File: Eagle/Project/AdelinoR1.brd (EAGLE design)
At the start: 47 x 53.3 mm, 63 parts, among them J1 DC-044-A, J2 YELLOW-6P-2.54, J3 YELLOW-8P-2.54, J4 YELLOW-8P-2.54, J5 YELLOW-8P-2.54, Q1 NCE3407A, Q2 CJ2305, U1 ATMEGA32U4-TQFP44, U2 CJT1117-5.0-SOT223, U3 ESP-12F / OPL: 317060163 / SM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, U4 CJT1117-3.3-SOT223, X1 306010049_XTAL_16MHZ-3225_4P

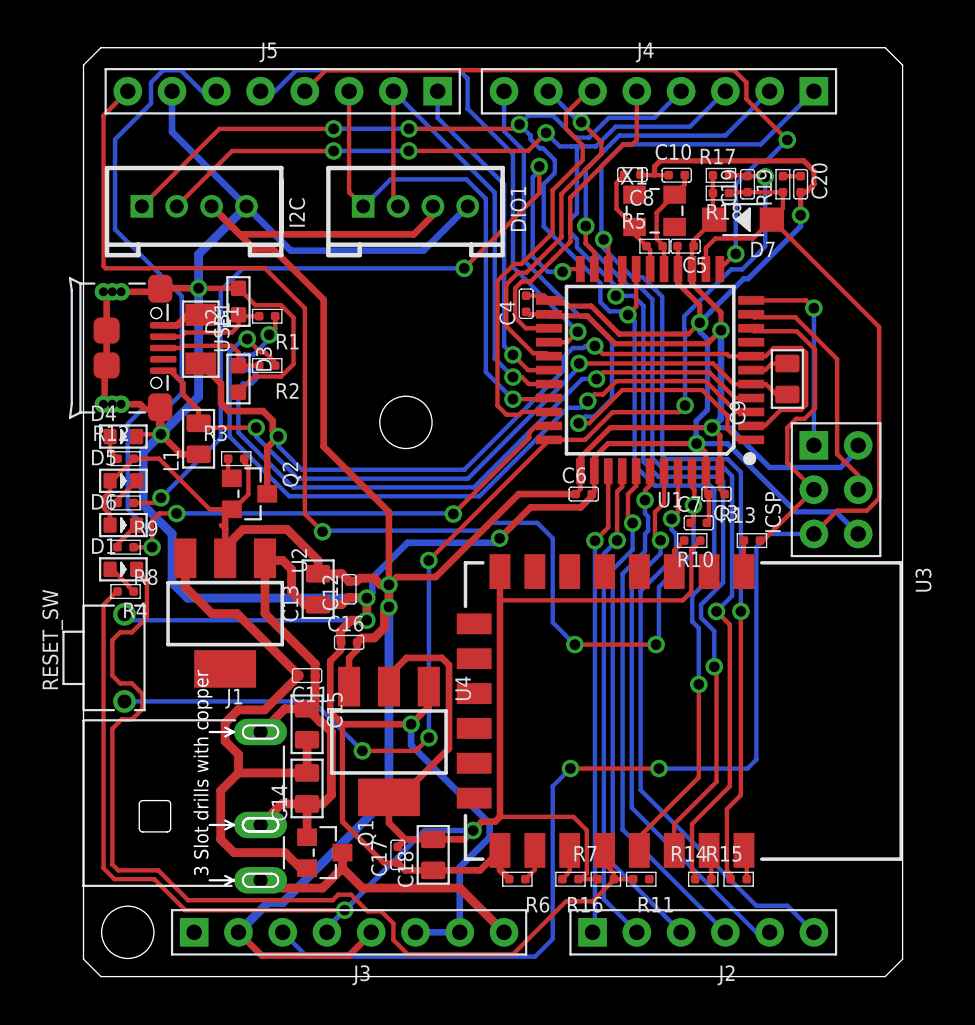
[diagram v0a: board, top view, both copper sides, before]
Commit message: Add MOSI->GPIO0 connection.
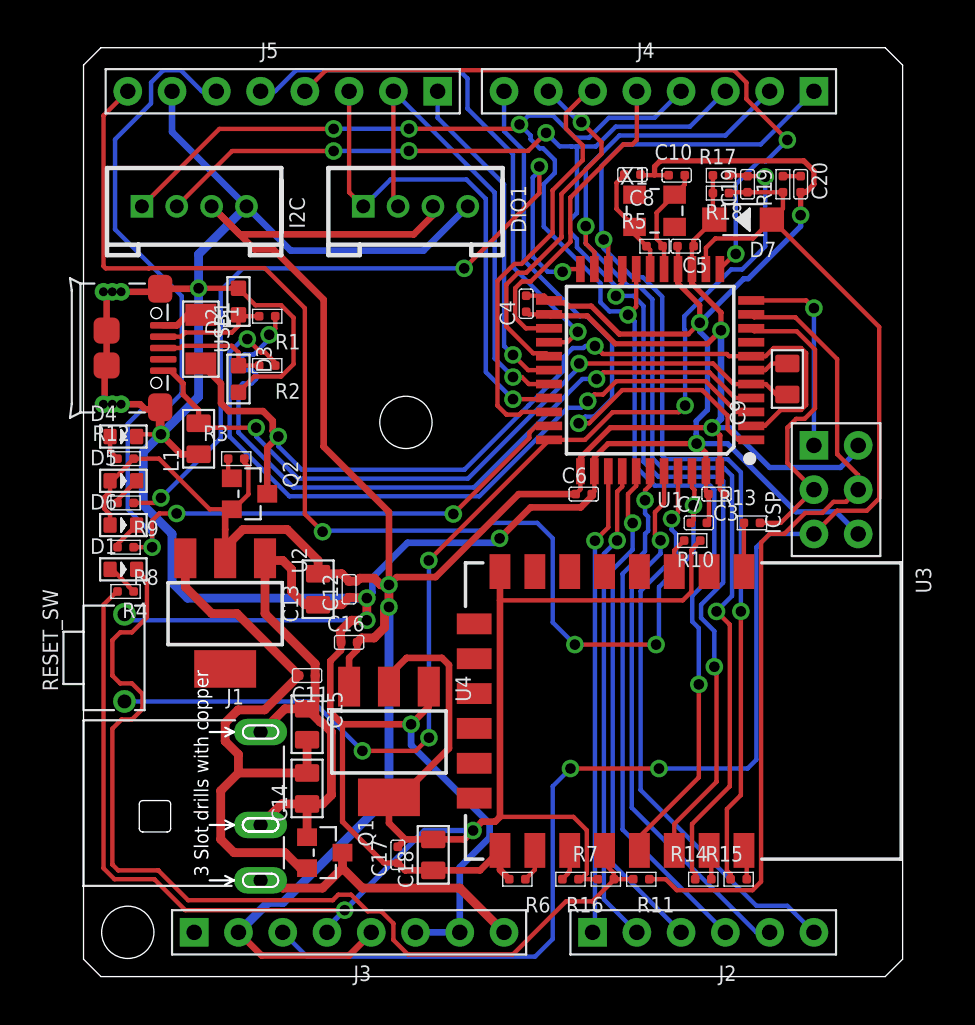
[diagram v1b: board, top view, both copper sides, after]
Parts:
- moved R13 1.02 mm to (38.4, 26.0)
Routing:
- net MOSI: track 14.0 -> 47.1 mm
- net N$14: track 1.78 -> 2.80 mm
- net GND: track 278.3 -> 278.8 mm
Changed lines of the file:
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@@
 <text x="18.0086" y="4.064" size="1.016" layer="136" font="vector" ratio="12">-GND-</text>
 <wire x1="13.97" y1="4.064" x2="13.97" y2="4.1148" width="0.1524" layer="136"/>
-<rectangle x1="38.862" y1="6.096" x2="46.99" y2="24.384" layer="41"/>
 <rectangle x1="38.862" y1="6.096" x2="46.99" y2="24.384" layer="42"/>
 <text x="4.064" y="31.877" size="0.8128" layer="136" font="vector" ratio="12" rot="SR270">PWR ACT D13 ESP</text>
@@
 www.neoautus.com
 Prototype only</text>
+<rectangle x1="39.116" y1="6.096" x2="46.99" y2="24.384" layer="41"/>
 </plain>
 <attributes>
@@
 <element name="C10" library="Seeed-Capacitor" package="C0402" value="22pf" x="34.036" y="45.9835" rot="R90">
 <attribute name="MPN" value="CC0402JRNPO9BN220" x="34.036" y="45.9835" size="1.778" layer="27" rot="R90" display="off"/>
+<attribute name="NAME" x="32.766" y="45.7295" size="0.635" layer="33" ratio="10"/>
 <attribute name="NAME" x="32.766" y="46.8725" size="0.889" layer="25" ratio="11"/>
-<attribute name="NAME" x="32.766" y="45.7295" size="0.635" layer="33" ratio="10"/>
 <attribute name="VALUE" x="32.766" y="44.396" size="0.635" layer="27" ratio="10"/>
 </element>
@@
 <element name="C8" library="Seeed-Capacitor" package="C0402" value="22pf" x="31.496" y="46.0195" rot="R270">
 <attribute name="MPN" value="CC0402JRNPO9BN220" x="31.496" y="46.0195" size="1.778" layer="27" rot="R270" display="off"/>
+<attribute name="NAME" x="32.766" y="46.2735" size="0.635" layer="33" ratio="10" rot="R180"/>
 <attribute name="NAME" x="32.766" y="45.1305" size="0.889" layer="25" ratio="11" rot="R180"/>
-<attribute name="NAME" x="32.766" y="46.2735" size="0.635" layer="33" ratio="10" rot="R180"/>
 <attribute name="VALUE" x="32.766" y="47.607" size="0.635" layer="27" ratio="10" rot="R180"/>
 </element>
@@
 <element name="J1" library="Seeed-Connector" package="DCJ3P-11.6X9.6X7.0MM" value="DC-044-A" x="0" y="9.906" rot="R270">
 <attribute name="MPN" value="JACK-DC-044-A" x="0" y="9.906" size="1.778" layer="27" rot="R270" display="off"/>
+<attribute name="NAME" x="6.985" y="13.1445" size="1.27" layer="33" ratio="10" rot="R270"/>
 <attribute name="NAME" x="8.1915" y="15.621" size="0.889" layer="25" ratio="11"/>
-<attribute name="NAME" x="6.985" y="13.1445" size="1.27" layer="33" ratio="10" rot="R270"/>
 <attribute name="VALUE" x="4.3815" y="3.556" size="0.889" layer="27" ratio="11"/>
 </element>
 <element name="J2" library="Seeed-Connector" package="H6-2.54" value="YELLOW-6P-2.54" x="35.56" y="2.54" rot="R90">
 <attribute name="MPN" value="F185-1106A1BSYA3" x="35.56" y="2.54" size="1.778" layer="27" rot="R90" display="off"/>
+<attribute name="NAME" x="38.1" y="3.175" size="0.635" layer="33" ratio="10" rot="R180"/>
 <attribute name="NAME" x="37.465" y="0.635" size="0.889" layer="25" ratio="11" rot="R180"/>
-<attribute name="NAME" x="38.1" y="3.175" size="0.635" layer="33" ratio="10" rot="R180"/>
 <attribute name="VALUE" x="37.465" y="5.08" size="0.889" layer="27" ratio="11" rot="R180"/>
 </element>
 <element name="J3" library="Seeed-Connector" package="H8-2.54" value="YELLOW-8P-2.54" x="15.24" y="2.54" rot="R90">
 <attribute name="MPN" value="F185-1108A1BSYC1" x="15.24" y="2.54" size="1.778" layer="27" rot="R90" display="off"/>
+<attribute name="NAME" x="15.875" y="2.54" size="0.3048" layer="33" ratio="10" rot="R180"/>
 <attribute name="NAME" x="16.51" y="0.635" size="0.889" layer="25" ratio="11" rot="R180"/>
-<attribute name="NAME" x="15.875" y="2.54" size="0.3048" layer="33" ratio="10" rot="R180"/>
 <attribute name="VALUE" x="16.51" y="5.08" size="0.889" layer="27" ratio="11" rot="R180"/>
 </element>
 <element name="J4" library="Seeed-Connector" package="H8-2.54" value="YELLOW-8P-2.54" x="33.02" y="50.8" rot="R270">
 <attribute name="MPN" value="F185-1108A1BSYC1" x="33.02" y="50.8" size="1.778" layer="27" rot="R270" display="off"/>
+<attribute name="NAME" x="32.385" y="50.8" size="0.3048" layer="33" ratio="10"/>
 <attribute name="NAME" x="31.75" y="52.705" size="0.889" layer="25" ratio="11"/>
-<attribute name="NAME" x="32.385" y="50.8" size="0.3048" layer="33" ratio="10"/>
 <attribute name="VALUE" x="31.75" y="48.26" size="0.889" layer="27" ratio="11"/>
 </element>
 <element name="J5" library="Seeed-Connector" package="H8-2.54" value="YELLOW-8P-2.54" x="11.43" y="50.8" rot="R270">
 <attribute name="MPN" value="F185-1108A1BSYC1" x="11.43" y="50.8" size="1.778" layer="27" rot="R270" display="off"/>
+<attribute name="NAME" x="10.795" y="50.8" size="0.3048" layer="33" ratio="10"/>
 <attribute name="NAME" x="10.16" y="52.705" size="0.889" layer="25" ratio="11"/>
-<attribute name="NAME" x="10.795" y="50.8" size="0.3048" layer="33" ratio="10"/>
 <attribute name="VALUE" x="10.16" y="48.26" size="0.889" layer="27" ratio="11"/>
 </element>
@@
 <attribute name="VALUE" x="0.808" y="28.283" size="0.635" layer="27" ratio="10"/>
 </element>
-<element name="R13" library="Seeed-Resistor" package="R0402" value="4.7K" x="38.354" y="25.019" rot="R270">
-<attribute name="MPN" value="RC0402JR-074K7L" x="38.354" y="25.019" size="1.778" layer="27" rot="R270" display="off"/>
-<attribute name="NAME" x="36.449" y="26.035" size="0.889" layer="25" ratio="11"/>
-<attribute name="VALUE" value="4.7K" x="36.749" y="23.584" size="0.635" layer="27" ratio="10"/>
+<element name="R13" library="Seeed-Resistor" package="R0402" value="4.7K" x="38.354" y="26.035" rot="R270">
+<attribute name="MPN" value="RC0402JR-074K7L" x="38.354" y="26.035" size="1.778" layer="27" rot="R270" display="off"/>
+<attribute name="NAME" x="36.449" y="27.051" size="0.889" layer="25" ratio="11"/>
+<attribute name="VALUE" value="4.7K" x="36.749" y="24.6" size="0.635" layer="27" ratio="10"/>
 </element>
 <element name="R14" library="Seeed-Resistor" package="R0402" value="4.7K" x="35.56" y="5.588" rot="R270">
@@
 <wire x1="4.399" y1="39.468" x2="4.2248" y2="39.2938" width="0.381" layer="1"/>
 <wire x1="4.2248" y1="39.2938" x2="2.159" y2="39.2938" width="0.381" layer="1"/>
-<wire x1="6.604" y1="39.497" x2="4.9022625" y2="39.497" width="0.381" layer="1"/>
 <wire x1="29.312" y1="28.998" x2="29.312" y2="29.79173125" width="0.3048" layer="1"/>
 <wire x1="35.179" y1="30.5816" x2="30.10186875" y2="30.5816" width="0.3048" layer="1"/>
@@
 <wire x1="5.969" y1="21.717" x2="5.08" y2="22.606" width="0.508" layer="16"/>
 <wire x1="5.969" y1="21.717" x2="16.256" y2="21.717" width="0.508" layer="16"/>
+<wire x1="4.399" y1="39.468" x2="6.575" y2="39.468" width="0.381" layer="1"/>
+<wire x1="6.575" y1="39.468" x2="6.604" y2="39.497" width="0.381" layer="1"/>
 </signal>
 <signal name="N$1">
@@
 <wire x1="9.4625" y1="29.2568125" x2="9.4625" y2="27.6711875" width="0.254" layer="1"/>
 <wire x1="9.4625" y1="27.6711875" x2="8.6043125" y2="26.813" width="0.254" layer="1"/>
-<wire x1="8.128" y1="25.654" x2="7.874" y2="25.908" width="0.254" layer="1"/>
 <wire x1="8.51" y1="26.813" x2="7.24" y2="26.813" width="0.254" layer="1"/>
 <wire x1="7.24" y1="26.813" x2="4.335" y2="29.718" width="0.254" layer="1"/>
@@
 <wire x1="40.386" y1="31.496" x2="40.386" y2="29.464" width="0.254" layer="1"/>
 <wire x1="40.386" y1="29.464" x2="41.91" y2="27.94" width="0.254" layer="1"/>
-<wire x1="41.91" y1="27.94" x2="38.989" y2="25.019" width="0.254" layer="1"/>
-<wire x1="38.989" y1="25.019" x2="38.8165" y2="25.019" width="0.254" layer="1"/>
+<wire x1="41.91" y1="27.94" x2="40.005" y2="26.035" width="0.254" layer="1"/>
+<wire x1="40.005" y1="26.035" x2="38.8165" y2="26.035" width="0.254" layer="1"/>
 </signal>
 <signal name="MOSI">
@@
 <wire x1="40.84376875" y1="37.829" x2="43.2435" y2="35.42926875" width="0.254" layer="1"/>
 <wire x1="43.2435" y1="35.42926875" x2="43.2435" y2="29.98025" width="0.254" layer="1"/>
-<wire x1="32.4665" y1="5.588" x2="44.45" y2="27.94" width="0" layer="19" extent="1-1"/>
+<wire x1="44.45" y1="27.94" x2="43.7515" y2="27.2415" width="0.254" layer="1"/>
+<wire x1="43.7515" y1="27.2415" x2="43.033075" y2="27.2415" width="0.254" layer="1"/>
+<wire x1="42.398075" y1="26.6065" x2="41.41025" y2="26.6065" width="0.254" layer="1"/>
+<wire x1="43.033075" y1="27.2415" x2="42.398075" y2="26.6065" width="0.254" layer="1"/>
+<wire x1="38.878" y1="5.44590625" x2="38.38909375" y2="4.957" width="0.254" layer="1"/>
+<wire x1="38.38909375" y1="4.957" x2="34.0411875" y2="4.957" width="0.254" layer="1"/>
+<wire x1="34.0411875" y1="4.957" x2="33.4101875" y2="5.588" width="0.254" layer="1"/>
+<wire x1="33.4101875" y1="5.588" x2="32.4665" y2="5.588" width="0.254" layer="1"/>
+<wire x1="41.41025" y1="26.6065" x2="40.20375" y2="25.4" width="0.254" layer="1"/>
+<wire x1="40.20375" y1="25.4" x2="39.37" y2="25.4" width="0.254" layer="1"/>
+<wire x1="39.37" y1="25.4" x2="38.878" y2="24.908" width="0.254" layer="1"/>
+<wire x1="38.878" y1="24.908" x2="38.878" y2="5.44590625" width="0.254" layer="1"/>
 </signal>
 <signal name="MISO">
@@
 <contactref element="R13" pad="2"/>
 <contactref element="U3" pad="1"/>
-<wire x1="37.8915" y1="25.019" x2="37.8915" y2="23.2455" width="0.254" layer="1"/>
+<wire x1="37.8915" y1="26.035" x2="37.8915" y2="23.2455" width="0.254" layer="1"/>
 <wire x1="37.8915" y1="23.2455" x2="37.897" y2="23.24" width="0.254" layer="1"/>
 </signal>

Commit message: Renumbered parts.
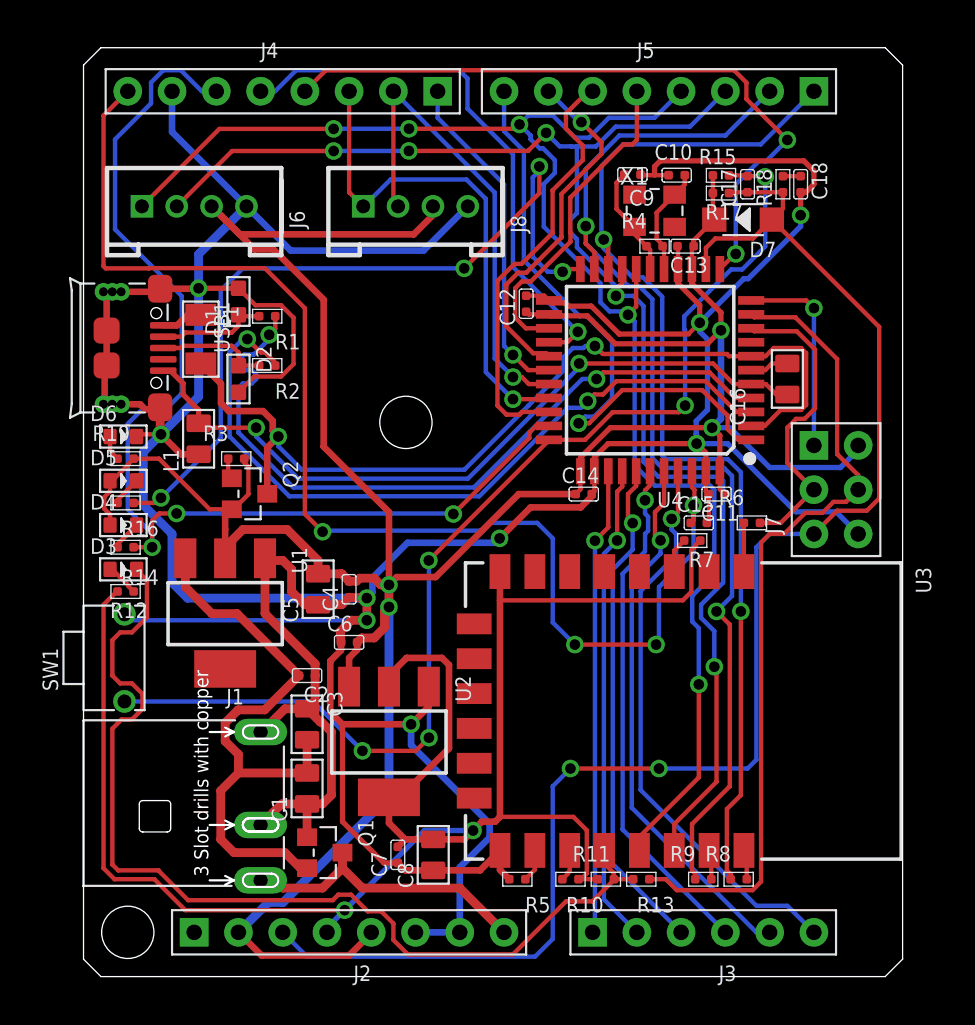
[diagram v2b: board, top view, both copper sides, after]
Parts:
- removed C19, C20: 100nf, Seeed-Capacitor:C0402
- added C1: 10uf, Seeed-Capacitor:C0805
- added C2: 100nf, Seeed-Capacitor:C0402
- C13, C14, C15, C18: value 10uf -> 100nf; device Seeed-Capacitor:C0805 -> Seeed-Capacitor:C0402
- C16: value 100nf -> 1uf; device Seeed-Capacitor:C0402 -> Seeed-Capacitor:C0805
- C3, C5: value 100nf -> 10uf; device Seeed-Capacitor:C0402 -> Seeed-Capacitor:C0805
- C8: value 22pf -> 10uf; device Seeed-Capacitor:C0402 -> Seeed-Capacitor:C0805
- C9: value 1uf -> 22pf; device Seeed-Capacitor:C0805 -> Seeed-Capacitor:C0402
- D1: value BLUE-0603 -> 1K 1/10W; device Seeed-LED:LED-0603 -> Seeed-Fuse:D0603
- D3: value 1K 1/10W -> BLUE-0603; device Seeed-Fuse:D0603 -> Seeed-LED:LED-0603
- D4: value GRE-0603 -> YEL-0603
- D6: value YEL-0603 -> GRE-0603
- J2: value YELLOW-6P-2.54 -> YELLOW-8P-2.54; device Seeed-Connector:H6-2.54 -> Seeed-Connector:H8-2.54
- J3: value YELLOW-8P-2.54 -> YELLOW-6P-2.54; device Seeed-Connector:H8-2.54 -> Seeed-Connector:H6-2.54
- R11: value 4.7K -> 10K
- R12: value 1K -> 470R
- R14, R16: value 4.7K -> 1K
- R15: value 4.7K -> 100K
- R18: value 100K -> 10K
- R19: value 10K -> 1K
- R4: value 470R -> 1M
- R5: value 1M -> 10K
- R6, R7: value 10K -> 4.7K
- R8, R9: value 1K -> 4.7K
- U1: value ATMEGA32U4-TQFP44 -> CJT1117-5.0-SOT223; device Seeed-IC:TQFP44-0.8-9.6X9.6MM -> Seeed-IC:SOT-223
- U2: value CJT1117-5.0-SOT223 -> CJT1117-3.3-SOT223
- U4: value CJT1117-3.3-SOT223 -> ATMEGA32U4-TQFP44; device Seeed-IC:SOT-223 -> Seeed-IC:TQFP44-0.8-9.6X9.6MM
- moved C18 43.9 mm to (41.1, 45.5), turned to 0 degrees
- moved C17 43.4 mm to (38.1, 45.5)
- moved R19 40.9 mm to (2.41, 29.7), turned to 270 degrees
- moved C8 40.7 mm to (20.1, 6.99), turned to 180 degrees
- moved R15 40.4 mm to (36.6, 46.0), turned to 90 degrees
- moved R8 40.0 mm to (37.6, 5.59), turned to 270 degrees
- moved R9 39.6 mm to (35.6, 5.59), turned to 270 degrees
- moved R14 38.2 mm to (2.41, 24.6), turned to 90 degrees
- moved R5 37.2 mm to (24.9, 5.59), turned to 90 degrees
- moved R4 36.2 mm to (32.8, 41.9)
- moved R16 33.4 mm to (2.41, 27.2)
- moved C16 29.3 mm to (40.4, 34.3), turned to 180 degrees
- moved C13 28.8 mm to (34.5, 41.9), turned to 270 degrees
- moved C5 28.8 mm to (13.5, 22.2), turned to 180 degrees
- moved U1 28.1 mm to (8.13, 20.8)
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- renumbered DIO1 to J8, I2C to J6, ICSP to J7, RESET_SW to SW1
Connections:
- net +3V3: now also C7.2, C8.2, J2.4, R10.2, R11.2, R12.2, R7.1, U2.2, U2.TER; no longer C17.2, C18.2, J3.4, R10.1, R16.2, R4.2, R7.2, U4.2, U4.TER
- net +5V: now also C11.1, C12.1, C13.1, C14.1, C4.2, C5.2, C6.2, D4.+, J2.2, J2.5, R15.1, R17.2, R19.1, U1.2, U1.TER, U2.3, U4.14, U4.24, U4.34, U4.44; no longer C12.2, C13.2, C16.2, C3.1, C4.1, C5.1, C6.1, D6.+, J3.2, J3.5, R12.1, R17.1, R18.2, U1.14, U1.24, U1.34, U1.44, U2.2, U2.TER, U4.3
- net D+: now also U4.4; no longer U1.4
- net D-: now also U4.3; no longer U1.3
- net ESP_EN: now also R7.2; no longer R10.2
- net GND: now also C1.1, C11.2, C12.2, C13.2, C14.2, C15.2, C18.2, C2.1, C3.1, C4.1, C5.1, C6.1, C7.1, C9.1, D1.1, D6.-, J2.6, J2.7, J4.7, R5.1, U1.1, U4.15, U4.23, U4.35, U4.43; no longer C11.1, C12.1, C13.1, C14.1, C15.1, C16.1, C17.1, C18.1, C20.2, C3.2, C4.2, C5.2, C6.2, C7.2, D3.1, D4.-, J3.6, J3.7, J5.7, R6.1, U1.15, U1.23, U1.35, U1.43, U4.1
- net GPIO0: now also D3.-, R13.1; no longer D1.-, R7.1
- net MISO: now also U4.11; no longer U1.11
- net MOSI: now also R13.2, U4.10; no longer R11.2, U1.10
- net N$1: now also D1.2; no longer D2.2
- net N$10: now also C1.2, C2.2, C3.2, U1.3; no longer C11.2, C14.2, C15.2, U2.3
- net N$11: now also R10.1; no longer R16.1
- net N$12: now also D3.+, R12.1; no longer D1.+, R4.1
- net N$13: now also C18.1, R18.2; no longer C20.1, R19.2
- net N$14: now also R6.2; no longer R13.2
- net N$17: now also R8.1; no longer R15.1
- net N$18: now also R9.1; no longer R14.1
- net N$2: now also D2.2; no longer D3.2
- net N$4: now also R5.2; no longer R6.2
- net N$5: now also D6.+, R19.2; no longer D4.+, R12.2
- net N$6: now also R16.1; no longer R9.1
- net N$7: now also C16.2, U4.6; no longer C9.2, U1.6
- net N$8: now also D4.-, R14.1; no longer D6.-, R8.1
- net PIN_A0: now also J3.1, U4.36; no longer J2.1, U1.36
- net PIN_A1: now also J3.2, U4.37; no longer J2.2, U1.37
- net PIN_A2: now also J3.3, U4.38; no longer J2.3, U1.38
- net PIN_A3: now also J3.4, U4.39; no longer J2.4, U1.39
- net PIN_A4: now also J3.5, U4.40; no longer J2.5, U1.40
- net PIN_A5: now also J3.6, U4.41; no longer J2.6, U1.41
- net PIN_AREF: now also C15.1, J4.8, U4.42; no longer C7.1, J5.8, U1.42
- net PIN_D0: now also J5.1, R8.2, U4.20; no longer J4.1, R15.2, U1.20
- net PIN_D1: now also J5.2, R9.2, U4.21; no longer J4.2, R14.2, U1.21
- net PIN_D10: now also J4.3, U4.30; no longer J5.3, U1.30
- net PIN_D11: now also J4.4, U4.12; no longer J5.4, U1.12
- net PIN_D12: now also J4.5, U4.26; no longer J5.5, U1.26
- net PIN_D13: now also J4.6, R14.2, U4.32; no longer J5.6, R8.2, U1.32
- net PIN_D2: now also J5.3, U4.19; no longer J4.3, U1.19
- net PIN_D3: now also J5.4, U4.18; no longer J4.4, U1.18
- net PIN_D4: now also J5.5, U4.25; no longer J4.5, U1.25
- net PIN_D5: now also J5.6, U4.31; no longer J4.6, U1.31
- net PIN_D6: now also J5.7, U4.27; no longer J4.7, U1.27
- net PIN_D7: now also J5.8, U4.1; no longer J4.8, U1.1
- net PIN_D8: now also J4.1, U4.28; no longer J5.1, U1.28
- net PIN_D9: now also J4.2, U4.29; no longer J5.2, U1.29
- net RESET: now also C17.1, J2.3, R17.1, U4.13; no longer C19.1, J3.3, R19.1, U1.13
- net RSTAT: now also C17.2, R15.2, U4.33; no longer C19.2, R17.2, U1.33
- net SCK: now also R6.1, U4.9; no longer R13.1, U1.9
- net SS: now also U4.8; no longer U1.8
- net TXLED: now also R16.2, U4.22; no longer R9.2, U1.22
- net UGND: now also C16.1, U4.5; no longer C9.1, U1.5
- net VIN: now also J2.8; no longer J3.8
- net VUSB: now also U4.2, U4.7; no longer U1.2, U1.7
- net XTAL1: now also C9.2, R4.2, U4.17; no longer C8.2, R5.2, U1.17
- net XTAL2: now also R4.1, U4.16; no longer R5.1, U1.16
